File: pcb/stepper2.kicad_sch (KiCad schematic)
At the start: 58 parts, among them J1 DA15_Receptacle_MountingHoles, J10 Conn_01x07_Pin, J11 FAN, J12 Conn_01x03_Pin, J13 Conn_01x03_Pin, J14 Conn_01x03_Pin, J2 DA15_Receptacle_MountingHoles, J3 DA15_Receptacle_MountingHoles, J4 DE15_Receptacle_HighDensity, J5 DE15_Receptacle_HighDensity, J6 DE15_Receptacle_HighDensity, J7 Conn_01x04_Pin, J8 Conn_01x05_Pin, J9 Conn_01x06_Pin, SW1 SW_Push, U1 AM26LS32ACN, U2 AM26LS32Ax, U3 AM26LS32ACN, U4 TMC2209_BIGTREETECH, U5 TMC2209_BIGTREETECH, U6 TMC2209_BIGTREETECH

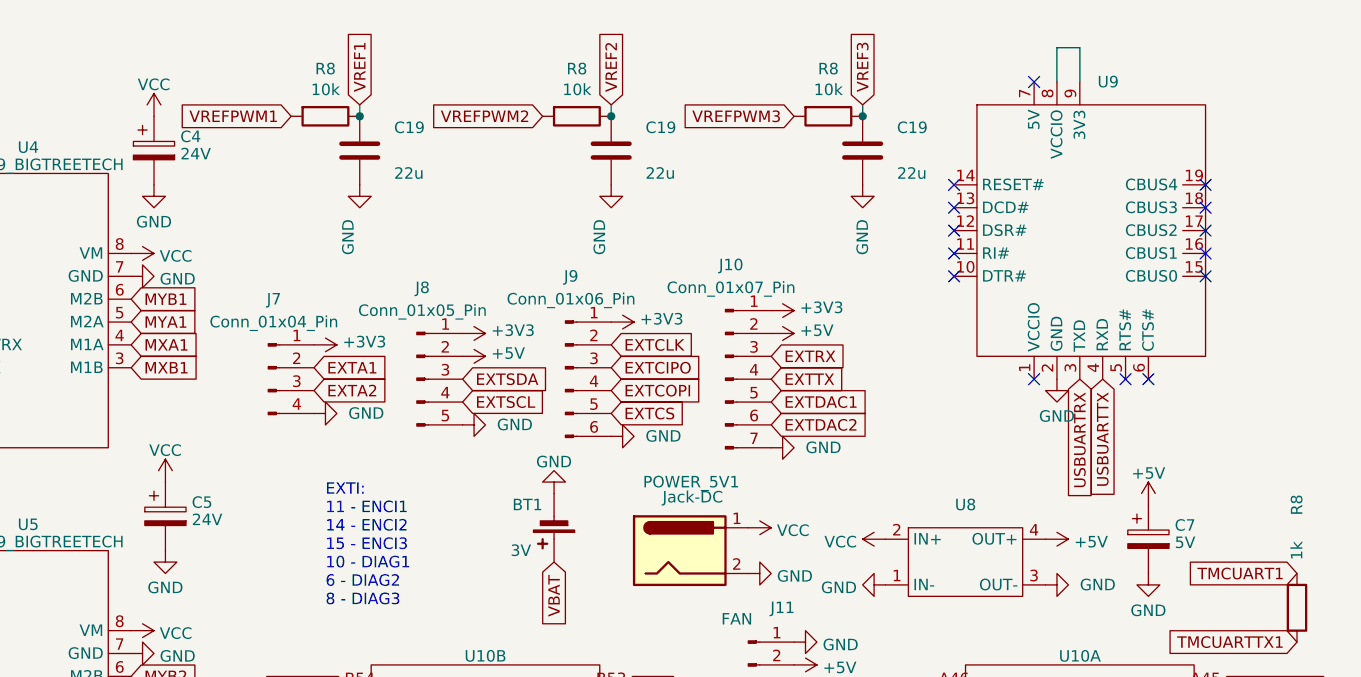
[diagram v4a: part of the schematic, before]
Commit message: Added voltage shifter between FTDI and board
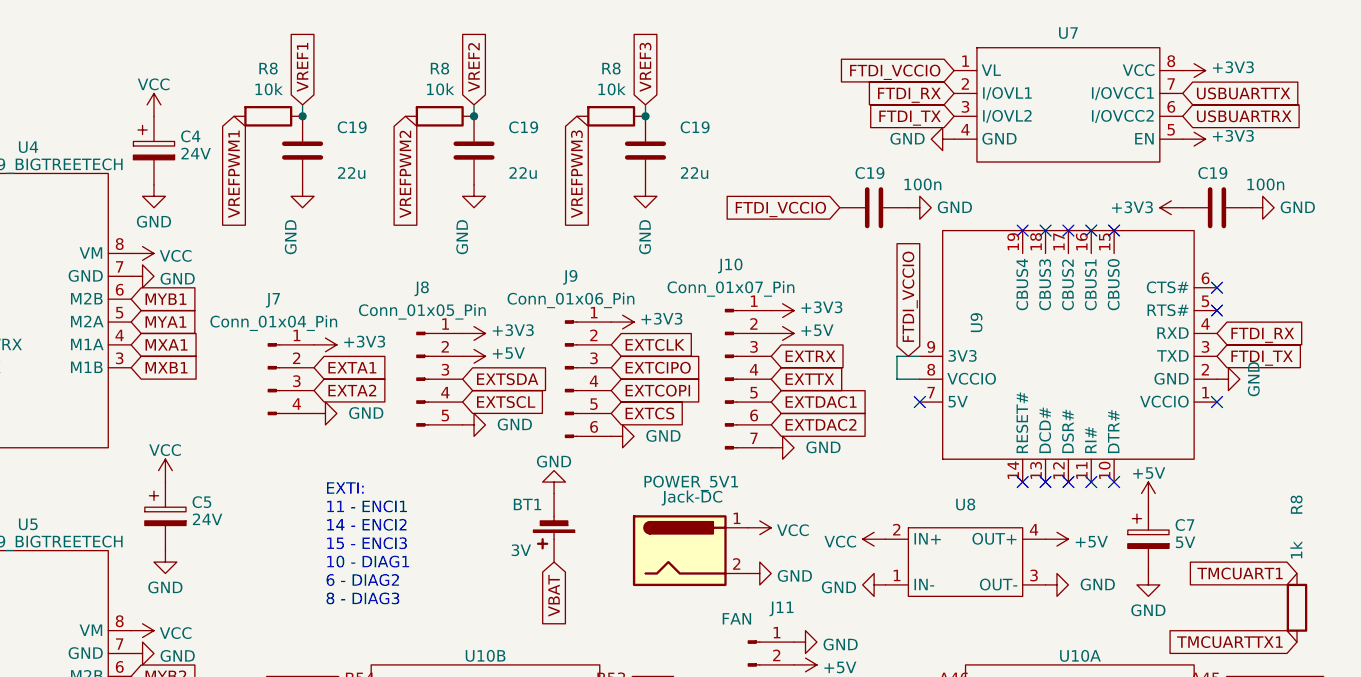
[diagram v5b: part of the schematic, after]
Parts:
- added C19 (x2): 100n, Capacitor_SMD:C_1206_3216Metric_Pad1.33x1.80mm_HandSolder, symbol Device:C
- added U7: ~, Package_DFN_QFN:OnSemi_UDFN-8_1.2x1.8mm_P0.4mm, symbol stepper2:NLSX4373MUTAG
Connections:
- net +3V3: now also C19.1, U7.5 (EN), U7.8 (VCC)
- net GND: now also C19.2, C19.2, U7.4 (GND)
- net USBUARTRX: now also U7.6 (I/OVCC2); no longer U9.3 (TXD)
- net USBUARTTX: now also U7.7 (I/OVCC1); no longer U9.4 (RXD)
- net FTDI_VCCIO: now reaches U9.8 (VCCIO), U9.9 (3V3)
- net FTDI_VCCIO: now also C19.1, U7.1 (VL)
- new net FTDI_RX: U7.2 (I/OVL1), U9.4 (RXD)
- new net FTDI_TX: U7.3 (I/OVL2), U9.3 (TXD)
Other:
- moved on the sheet: C19, R8, U9

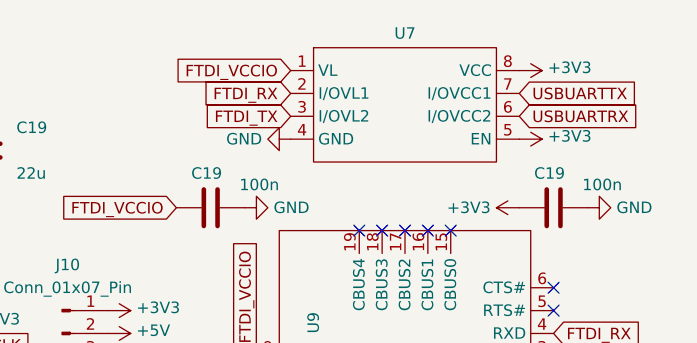
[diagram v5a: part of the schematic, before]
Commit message: universal footprint for UART level shifter
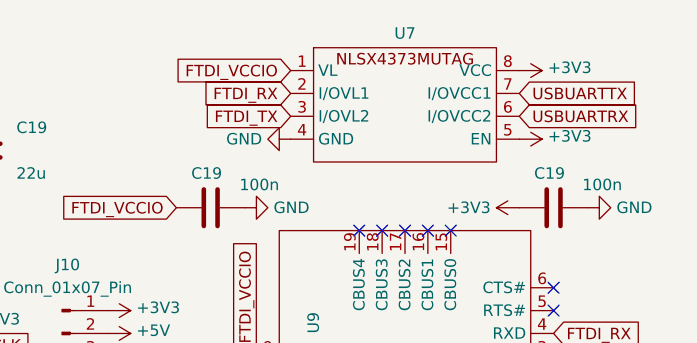
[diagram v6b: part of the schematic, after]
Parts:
- U7: footprint Package_DFN_QFN:OnSemi_UDFN-8_1.2x1.8mm_P0.4mm -> stepper2:UDFN-8_1.2x1.8mm_OR_SO8_3.9x4.9mm
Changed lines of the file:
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@@
       (effects (font (size 1.27 1.27)))
     )
-    (property "Footprint" "Package_DFN_QFN:OnSemi_UDFN-8_1.2x1.8mm_P0.4mm" (at 255.27 21.59 0)
+    (property "Footprint" "stepper2:UDFN-8_1.2x1.8mm_OR_SO8_3.9x4.9mm" (at 255.27 21.59 0)
       (effects (font (size 1.27 1.27)) hide)
     )

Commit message: top part of the case, adjustments to the PCB
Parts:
- SW1: LCSC C455126 -> C620327
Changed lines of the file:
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@@
       (effects (font (size 1.27 1.27)) hide)
     )
-    (property "LCSC" "C455126" (at 160.02 185.42 0)
+    (property "LCSC" "C620327" (at 160.02 185.42 0)
       (effects (font (size 1.27 1.27)) hide)
     )
@@
       (effects (font (size 1.27 1.27)) hide)
     )
-    (property "LCSC" "C455126" (at 160.02 160.02 0)
+    (property "LCSC" "C620327" (at 160.02 160.02 0)
       (effects (font (size 1.27 1.27)) hide)
     )
@@
       (effects (font (size 1.27 1.27)) hide)
     )
-    (property "LCSC" "C455126" (at 160.02 172.72 0)
+    (property "LCSC" "C620327" (at 160.02 172.72 0)
       (effects (font (size 1.27 1.27)) hide)
     )
@@
       (effects (font (size 1.27 1.27)) hide)
     )
-    (property "LCSC" "C455126" (at 132.08 185.42 0)
+    (property "LCSC" "C620327" (at 132.08 185.42 0)
       (effects (font (size 1.27 1.27)) hide)
     )
@@
       (effects (font (size 1.27 1.27)) hide)
     )
-    (property "LCSC" "C455126" (at 132.08 160.02 0)
+    (property "LCSC" "C620327" (at 132.08 160.02 0)
       (effects (font (size 1.27 1.27)) hide)
     )
@@
       (effects (font (size 1.27 1.27)) hide)
     )
-    (property "LCSC" "C455126" (at 132.08 172.72 0)
-      (effects (font (size 1.27 1.27)) hide)
-    )
+    (property "LCSC" "C620327" (at 132.08 172.72 0)
+      (effects (font (size 1.27 1.27)) hide)
+    )

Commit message: last fixes and production files for pcb
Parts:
- J10: LCSC C2856758 -> C265453
- J12, J13, J14: LCSC C2688785 -> C265101
- J7: LCSC C2688786 -> C265102
- J8: LCSC C2874530 -> C265104
- J9: LCSC C2874531 -> C265405
- U1, U2, U3: LCSC (none) -> C19092
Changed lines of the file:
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@@
       (effects (font (size 1.27 1.27)) hide)
     )
+    (property "LCSC" "C19092" (at 67.31 104.14 0)
+      (effects (font (size 1.27 1.27)) hide)
+    )
     (pin "1")
     (pin "10")
@@
       (effects (font (size 1.27 1.27)) hide)
     )
-    (property "LCSC" "C2874530" (at 182.88 52.07 0)
+    (property "LCSC" "C265104" (at 182.88 52.07 0)
       (effects (font (size 1.27 1.27)) hide)
     )
@@
       (effects (font (size 1.27 1.27)) hide)
     )
-    (property "LCSC" "C2856758" (at 217.17 52.07 0)
+    (property "LCSC" "C265453" (at 217.17 52.07 0)
       (effects (font (size 1.27 1.27)) hide)
     )
@@
       (effects (font (size 1.27 1.27)) hide)
     )
-    (property "LCSC" "C2688786" (at 166.37 50.8 0)
+    (property "LCSC" "C265102" (at 166.37 50.8 0)
       (effects (font (size 1.27 1.27)) hide)
     )
@@
       (effects (font (size 1.27 1.27)) hide)
     )
-    (property "LCSC" "C2688785" (at 99.06 170.18 0)
+    (property "LCSC" "C265101" (at 99.06 170.18 0)
       (effects (font (size 1.27 1.27)) hide)
     )
@@
       (effects (font (size 1.27 1.27)) hide)
     )
-    (property "LCSC" "C2688785" (at 99.06 185.42 0)
+    (property "LCSC" "C265101" (at 99.06 185.42 0)
       (effects (font (size 1.27 1.27)) hide)
     )
@@
       (effects (font (size 1.27 1.27)) hide)
     )
-    (property "LCSC" "C2688785" (at 99.06 154.94 0)
+    (property "LCSC" "C265101" (at 99.06 154.94 0)
       (effects (font (size 1.27 1.27)) hide)
     )
@@
       (effects (font (size 1.27 1.27)) hide)
     )
+    (property "LCSC" "C19092" (at 67.31 44.45 0)
+      (effects (font (size 1.27 1.27)) hide)
+    )
     (pin "1")
     (pin "10")
@@
       (effects (font (size 1.27 1.27)) hide)
     )
+    (property "LCSC" "C19092" (at 67.31 166.37 0)
+      (effects (font (size 1.27 1.27)) hide)
+    )
     (pin "1")
     (pin "10")
@@
       (effects (font (size 1.27 1.27)) hide)
     )
-    (property "LCSC" "C2874531" (at 199.39 50.8 0)
+    (property "LCSC" "C265405" (at 199.39 50.8 0)
       (effects (font (size 1.27 1.27)) hide)
     )
